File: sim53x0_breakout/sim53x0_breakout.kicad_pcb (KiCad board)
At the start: 2 copper layers, 40 x 43 mm, 35 parts, among them J1 CONN_01X05, J2 USB_OTG, J4 CONN_01X06, U1 SIM5320

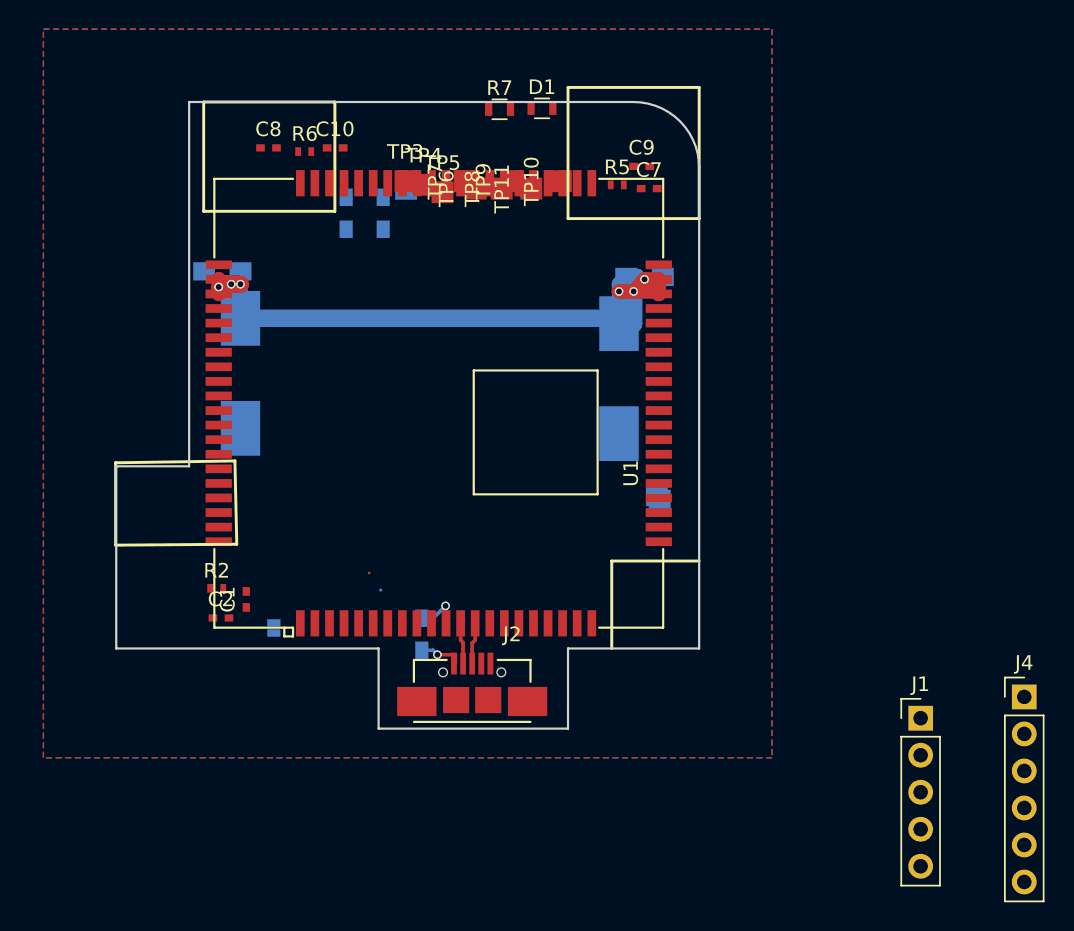
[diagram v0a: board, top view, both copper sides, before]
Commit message: Adding u.FL to SIM53x0 board - no antenna traces yet
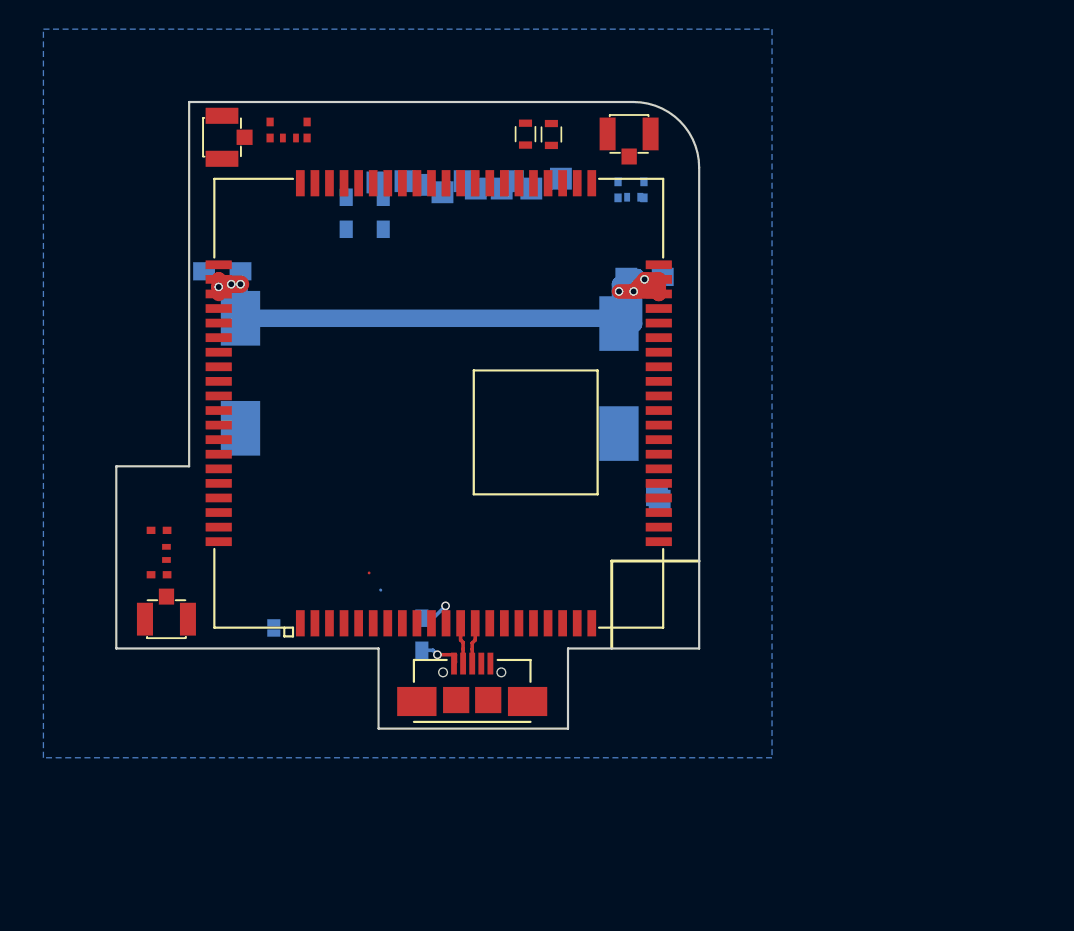
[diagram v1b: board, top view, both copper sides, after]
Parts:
- removed J1: CONN_01X05, Pin_Headers:Pin_Header_Straight_1x05_Pitch2.54mm
- removed J4: CONN_01X06, Pin_Headers:Pin_Header_Straight_1x06_Pitch2.54mm
- added J5: CONN_COAXIAL, footprints:HRS_U.FL-R-SMT(01), F.Cu at (123.4, 110.5)
- added J8: CONN_COAXIAL, footprints:HRS_U.FL-R-SMT(01), F.Cu at (155.2, 77.2)
- added J9: CONN_COAXIAL, footprints:HRS_U.FL-R-SMT(01), F.Cu at (127.3, 77.4)
- C7, C9, R5, TP10, TP11, TP3, TP4, TP5, TP6, TP7, TP8, TP9: moved to B.Cu
- moved C2 7.36 mm to (122.9, 104.4), turned to 180 degrees
- moved C1 6.22 mm to (122.9, 107.4), turned to 180 degrees
- moved C10 4.63 mm to (130.6, 76.9), turned to 90 degrees
- moved R2 4.20 mm to (123.4, 106.0), turned to 90 degrees
- moved C8 2.92 mm to (133.1, 76.9), turned to 90 degrees
- moved R7 2.46 mm to (148.1, 77.2), turned to 90 degrees
- moved C9 2.29 mm to (154.4, 81.0), turned to 270 degrees
- moved TP12 2.02 mm to (137.9, 80.5)
- moved D1 1.90 mm to (149.9, 77.2), turned to 270 degrees
- moved R5 1.41 mm to (155.5, 81.5)
- moved R6 1.40 mm to (131.9, 77.5)
- moved C7 0.37 mm to (156.2, 81.0), turned to 90 degrees
- moved TP10 0.17 mm to (150.5, 80.3), turned to 270 degrees
- turned TP11 to 270 degrees
- turned TP6 to 270 degrees
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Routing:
- removed copper zone on F.Cu, net GND

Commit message: New version of the SIM5X30 breakout - adjusted for Delta boards
Needs to be printed out to see clearances
No SIM slot footprint yet
No SIM5320, u.FL and SIM slot 3D models
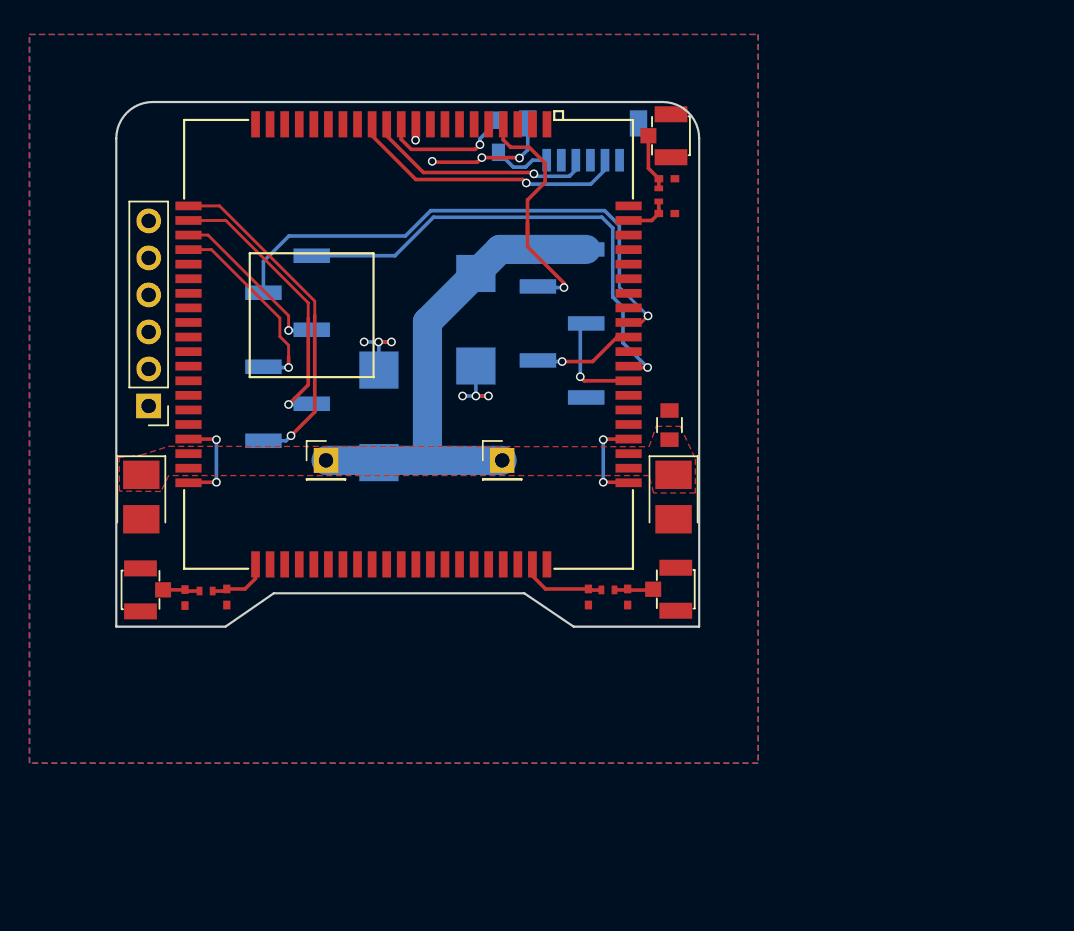
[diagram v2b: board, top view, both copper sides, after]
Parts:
- removed C6: 100nF, Capacitors_SMD:C_0805_HandSoldering
- removed D1: LED, Resistors_SMD:R_0603
- removed J2: USB_OTG, footprints:MICROUSB_SIMPLE
- removed JP1: PWRKEY, footprints:GS2_SMALL
- removed R3, R4: 4.7K, Resistors_SMD:R_0603_HandSoldering
- removed R7: R_Small, Resistors_SMD:R_0603
- removed TP1: EAR-, Measurement_Points:Measurement_Point_Square-SMD-Pad_Small
- removed TP10: VRTC, Measurement_Points:Measurement_Point_Square-SMD-Pad_Small
- removed TP11: VDD_IO, Measurement_Points:Measurement_Point_Square-SMD-Pad_Small
- removed TP12: GPIO42, Measurement_Points:Measurement_Point_Square-SMD-Pad_Small
- removed TP2: EAR+, Measurement_Points:Measurement_Point_Square-SMD-Pad_Small
- removed TP5: GPIO43, Measurement_Points:Measurement_Point_Square-SMD-Pad_Small
- removed TP6: GPIO40, Measurement_Points:Measurement_Point_Square-SMD-Pad_Small
- removed TP7: GPIO44, Measurement_Points:Measurement_Point_Square-SMD-Pad_Small
- removed TP8: ADC1, Measurement_Points:Measurement_Point_Square-SMD-Pad_Small
- removed TP9: ADC2, Measurement_Points:Measurement_Point_Square-SMD-Pad_Small
- added C11: 10nF, Capacitors_Tantalum_SMD:CP_Tantalum_Case-B_EIA-3528-21_Reflow, F.Cu at (158.2, 102.1)
- added C12: 10nF, Capacitors_Tantalum_SMD:CP_Tantalum_Case-B_EIA-3528-21_Reflow, F.Cu at (121.7, 102.1)
- added J1: CONN_01X05, Pin_Headers:Pin_Header_Straight_1x05_Pitch2.54mm_SMD_Pin1Left, B.Cu at (150.6, 90.2)
- added J4: CONN_01X06, Pin_Headers:Pin_Header_Straight_1x06_Pitch2.54mm_SMD_Pin1Left, B.Cu at (131.8, 91.9)
- added J6: Conn_01x06, Pin_Headers:Pin_Header_Straight_1x06_Pitch2.54mm, F.Cu at (122.2, 95.9)
- added J7: Conn_01x07, Connectors_JST:JST_SH_BM06B-SRSS-TB_06x1.00mm_Straight, B.Cu at (152.0, 77.7)
- C3, C5: footprint Capacitors_Tantalum_SMD:CP_Tantalum_Case-D_EIA-7343-31_Hand -> Capacitors_Tantalum_SMD:CP_Tantalum_Case-D_EIA-7343-31_Reflow
- C4: footprint Capacitors_SMD:C_0805_HandSoldering -> Capacitors_SMD:C_0805; moved to F.Cu
- C7, C9, R5: moved to F.Cu
- TP3: value GPIO4 -> TEST; footprint Measurement_Points:Measurement_Point_Square-SMD-Pad_Small -> Pin_Headers:Pin_Header_Straight_1x01_Pitch2.54mm; moved to F.Cu
- TP4: value GPIO41 -> TEST; footprint Measurement_Points:Measurement_Point_Square-SMD-Pad_Small -> Pin_Headers:Pin_Header_Straight_1x01_Pitch2.54mm; moved to F.Cu
- moved J5 47.9 mm to (158.1, 77.3), turned to 270 degrees
- moved J8 45.9 mm to (121.7, 108.5), turned to 90 degrees
- moved C1 44.2 mm to (157.8, 80.3), turned to 0 degrees
- moved J9 43.9 mm to (158.4, 108.4), turned to 270 degrees
- moved R2 41.8 mm to (157.2, 81.4), turned to 270 degrees
- moved C2 41.1 mm to (157.8, 82.7), turned to 0 degrees
- moved C9 40.8 mm to (124.7, 109.0)
- moved C10 40.4 mm to (155.1, 109.0), turned to 270 degrees
- moved C7 40.0 mm to (127.6, 109.0), turned to 270 degrees
- moved R5 39.9 mm to (126.2, 108.6)
- moved R6 37.9 mm to (153.7, 108.5), turned to 180 degrees
- moved C8 37.4 mm to (152.4, 109.0), turned to 270 degrees
- moved R1 34.6 mm to (146.2, 77.4)
- moved C4 32.5 mm to (158.0, 97.2), turned to 90 degrees
- moved TP3 19.9 mm to (134.4, 99.6)
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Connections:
- TP3 pad 1: Net-(TP3-Pad1) -> VDD
- TP4 pad 1: Net-(TP4-Pad1) -> VDD
- U1 pad 25: Net-(TP1-Pad1) -> (no net)
- U1 pad 26: Net-(TP2-Pad1) -> (no net)
- U1 pad 42: Net-(TP10-Pad1) -> (no net)
- U1 pad 44: VDD_IO -> (no net)
- U1 pad 46: Net-(TP9-Pad1) -> (no net)
- U1 pad 47: Net-(TP8-Pad1) -> (no net)
- U1 pad 48: Net-(TP7-Pad1) -> (no net)
- U1 pad 49: Net-(TP6-Pad1) -> (no net)
- U1 pad 50: Net-(TP5-Pad1) -> (no net)
- U1 pad 51: Net-(D1-Pad2) -> (no net)
- U1 pad 52: Net-(TP4-Pad1) -> (no net)
- U1 pad 53: GPIO42 -> (no net)
- U1 pad 54: Net-(TP3-Pad1) -> (no net)
- U1 pad 55: SCL -> (no net)
- U1 pad 56: SDA -> (no net)
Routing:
- net DTR: track 0.00 -> 37.3 mm, vias 0 -> 1
- net RING: track 0.00 -> 34.0 mm, vias 0 -> 1
- net GND: track 0.00 -> 32.5 mm, vias 0 -> 14
- net SPK-: track 0.00 -> 23.3 mm, vias 0 -> 1
- net SPK+: track 0.00 -> 19.7 mm, vias 0 -> 1
- net VDD: track 56.7 -> 38.3 mm, vias 6 -> 0
- net RESET: track 0.00 -> 17.2 mm, vias 0 -> 1
- net /D+: track 2.85 -> 19.2 mm, vias 0 -> 1
- net MIC-: track 0.00 -> 13.6 mm, vias 0 -> 1
- net /D-: track 2.84 -> 15.8 mm, vias 0 -> 1
- net MIC+: track 0.00 -> 11.8 mm, vias 0 -> 1
- net RXD: track 0.00 -> 7.36 mm, vias 0 -> 1
- net TXD: track 0.00 -> 6.95 mm, vias 0 -> 1
- net /MAIN_ANT: track 0.00 -> 5.92 mm
- net Net-(R1-Pad1): track 3.19 -> 9.05 mm
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- added copper zone on F.Cu, net GND
- added copper zone on F.Cu, net VDD
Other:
- board size 40 x 43 mm -> 40 x 36 mm
